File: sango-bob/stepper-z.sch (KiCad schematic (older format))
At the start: 27 parts, among them P801 CONN_8, P802 CONN_8, P803 MOT_Z, P804 MOT_Z, U801 A4985-LP

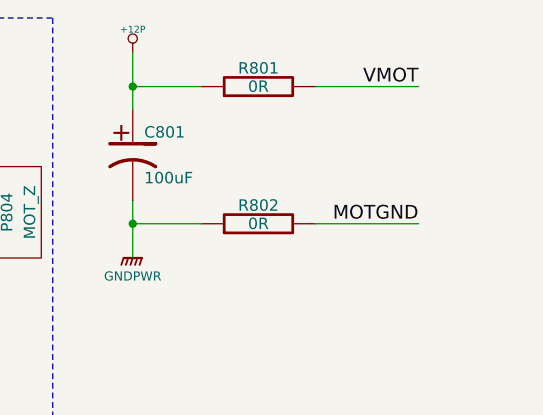
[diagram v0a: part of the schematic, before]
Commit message: Updates to symbols and fix some ERC errors
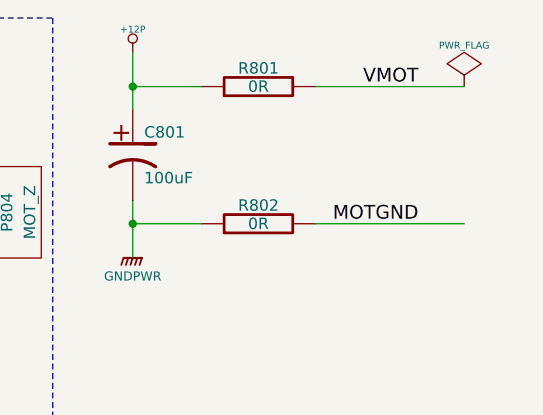
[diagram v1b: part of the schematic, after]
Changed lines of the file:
@@
-EESchema Schematic File Version 2  date 03/01/2013 13:12:05
+EESchema Schematic File Version 2  date 22/01/2013 21:21:55
 LIBS:power
 LIBS:device
@@
 Sheet 8 9
 Title ""
-Date "2 jan 2013"
+Date "22 jan 2013"
 Rev ""
 Comp ""
@@
 Comment4 ""
 $EndDescr
+Wire Wire Line
+	8750 900  8100 900
 Connection ~ 4850 5150
 Wire Wire Line
@@
 Wire Wire Line
 	8000 4800 7950 4800
-Wire Wire Line
-	8550 1500 8100 1500
-Wire Wire Line
-	8550 900  8100 900
 Connection ~ 4100 4050
 Wire Wire Line
@@
 Wire Wire Line
 	5650 1100 5250 1100
+Wire Wire Line
+	8750 1500 8100 1500
+$Comp
+L PWR_FLAG #FLG096
+U 1 1 50FEFF09
+P 8750 900
+F 0 "#FLG096" H 8750 995 30  0001 C CNN
+F 1 "PWR_FLAG" H 8750 1080 30  0000 C CNN
+	1    8750 900
+	1    0    0    -1
+$EndComp
 $Comp
 L TEST_POINT_RMC TP801
@@
 $EndComp
 $Comp
-L VDD #PWR095
+L VDD #PWR097
 U 1 1 50DDCE0E
 P 2800 3300
-F 0 "#PWR095" H 2800 3400 30  0001 C CNN
+F 0 "#PWR097" H 2800 3400 30  0001 C CNN
 F 1 "VDD" H 2800 3410 30  0000 C CNN
 	1    2800 3300
@@
 $EndComp
 $Comp
-L GND #PWR096
+L GND #PWR098
 U 1 1 50E23BBD
 P 2800 4100
-F 0 "#PWR096" H 2800 4100 30  0001 C CNN
+F 0 "#PWR098" H 2800 4100 30  0001 C CNN
 F 1 "GND" H 2800 4030 30  0001 C CNN
 	1    2800 4100
@@
 $EndComp
 $Comp
-L VDD #PWR097
+L VDD #PWR099
 U 1 1 50E21158
 P 3300 1550
-F 0 "#PWR097" H 3300 1650 30  0001 C CNN
+F 0 "#PWR099" H 3300 1650 30  0001 C CNN
 F 1 "VDD" H 3300 1660 30  0000 C CNN
 	1    3300 1550
@@
 $EndComp
 $Comp
-L GND #PWR098
+L GND #PWR0100
 U 1 1 50E23B82
 P 6000 6150
-F 0 "#PWR098" H 6000 6150 30  0001 C CNN
+F 0 "#PWR0100" H 6000 6150 30  0001 C CNN
 F 1 "GND" H 6000 6080 30  0001 C CNN
 	1    6000 6150
@@
 $EndComp
 $Comp
-L GND #PWR099
+L GND #PWR0101
 U 1 1 50E21152
 P 5200 3500
-F 0 "#PWR099" H 5200 3500 30  0001 C CNN
+F 0 "#PWR0101" H 5200 3500 30  0001 C CNN
 F 1 "GND" H 5200 3430 30  0001 C CNN
 	1    5200 3500
@@
 $EndComp
 $Comp
-L GND #PWR0100
+L GND #PWR0102
 U 1 1 50E23BB3
 P 4550 5950
-F 0 "#PWR0100" H 4550 5950 30  0001 C CNN
+F 0 "#PWR0102" H 4550 5950 30  0001 C CNN
 F 1 "GND" H 4550 5880 30  0001 C CNN
 	1    4550 5950
@@
 $EndComp
 $Comp
-L GND #PWR0101
+L GND #PWR0103
 U 1 1 50E23B7B
 P 4100 5950
-F 0 "#PWR0101" H 4100 5950 30  0001 C CNN
+F 0 "#PWR0103" H 4100 5950 30  0001 C CNN
 F 1 "GND" H 4100 5880 30  0001 C CNN
 	1    4100 5950
@@
 $EndComp
 $Comp
-L VDD #PWR0102
+L VDD #PWR0104
 U 1 1 50E2114C
 P 4100 3850
-F 0 "#PWR0102" H 4100 3950 30  0001 C CNN
+F 0 "#PWR0104" H 4100 3950 30  0001 C CNN
 F 1 "VDD" H 4100 3960 30  0000 C CNN
 	1    4100 3850
@@
 $EndComp
 $Comp
-L GND #PWR0103
+L GND #PWR0105
 U 1 1 50E23BA6
 P 2550 6000
-F 0 "#PWR0103" H 2550 6000 30  0001 C CNN
+F 0 "#PWR0105" H 2550 6000 30  0001 C CNN
 F 1 "GND" H 2550 5930 30  0001 C CNN
 	1    2550 6000
@@
 MOTGND
 $Comp
-L VDD #PWR0104
+L VDD #PWR0106
 U 1 1 50D57F57
 P 5750 1700
-F 0 "#PWR0104" H 5750 1800 30  0001 C CNN
+F 0 "#PWR0106" H 5750 1800 30  0001 C CNN
 F 1 "VDD" H 5750 1810 30  0000 C CNN
 	1    5750 1700
@@
 $EndComp
 $Comp
-L +12P #PWR0105
+L +12P #PWR0107
 U 1 1 50E23BA3
 P 7300 750
-F 0 "#PWR0105" H 7300 720 30  0001 C CNN
+F 0 "#PWR0107" H 7300 720 30  0001 C CNN
 F 1 "+12P" H 7300 850 30  0000 C CNN
 	1    7300 750
@@
 $EndComp
 $Comp
-L VDD #PWR0106
+L VDD #PWR0108
 U 1 1 50E23B70
 P 2300 950
-F 0 "#PWR0106" H 2300 1050 30  0001 C CNN
+F 0 "#PWR0108" H 2300 1050 30  0001 C CNN
 F 1 "VDD" H 2300 1060 30  0000 C CNN
 	1    2300 950
@@
 $EndComp
 $Comp
-L GND #PWR0107
+L GND #PWR0109
 U 1 1 50E2113C
 P 5550 2250
-F 0 "#PWR0107" H 5550 2250 30  0001 C CNN
+F 0 "#PWR0109" H 5550 2250 30  0001 C CNN
 F 1 "GND" H 5550 2180 30  0001 C CNN
 	1    5550 2250
@@
 $EndComp
 $Comp
-L GND #PWR0108
+L GND #PWR0110
 U 1 1 50E23B8E
 P 2800 2300
-F 0 "#PWR0108" H 2800 2300 30  0001 C CNN
+F 0 "#PWR0110" H 2800 2300 30  0001 C CNN
 F 1 "GND" H 2800 2230 30  0001 C CNN
 	1    2800 2300
@@
 $EndComp
 $Comp
-L GNDPWR #PWR0109
+L GNDPWR #PWR0111
 U 1 1 50E21135
 P 7300 1650
-F 0 "#PWR0109" H 7300 1700 40  0001 C CNN
+F 0 "#PWR0111" H 7300 1700 40  0001 C CNN
 F 1 "GNDPWR" H 7300 1570 40  0000 C CNN
 	1    7300 1650
